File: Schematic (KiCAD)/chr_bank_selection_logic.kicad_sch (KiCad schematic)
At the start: 44 parts

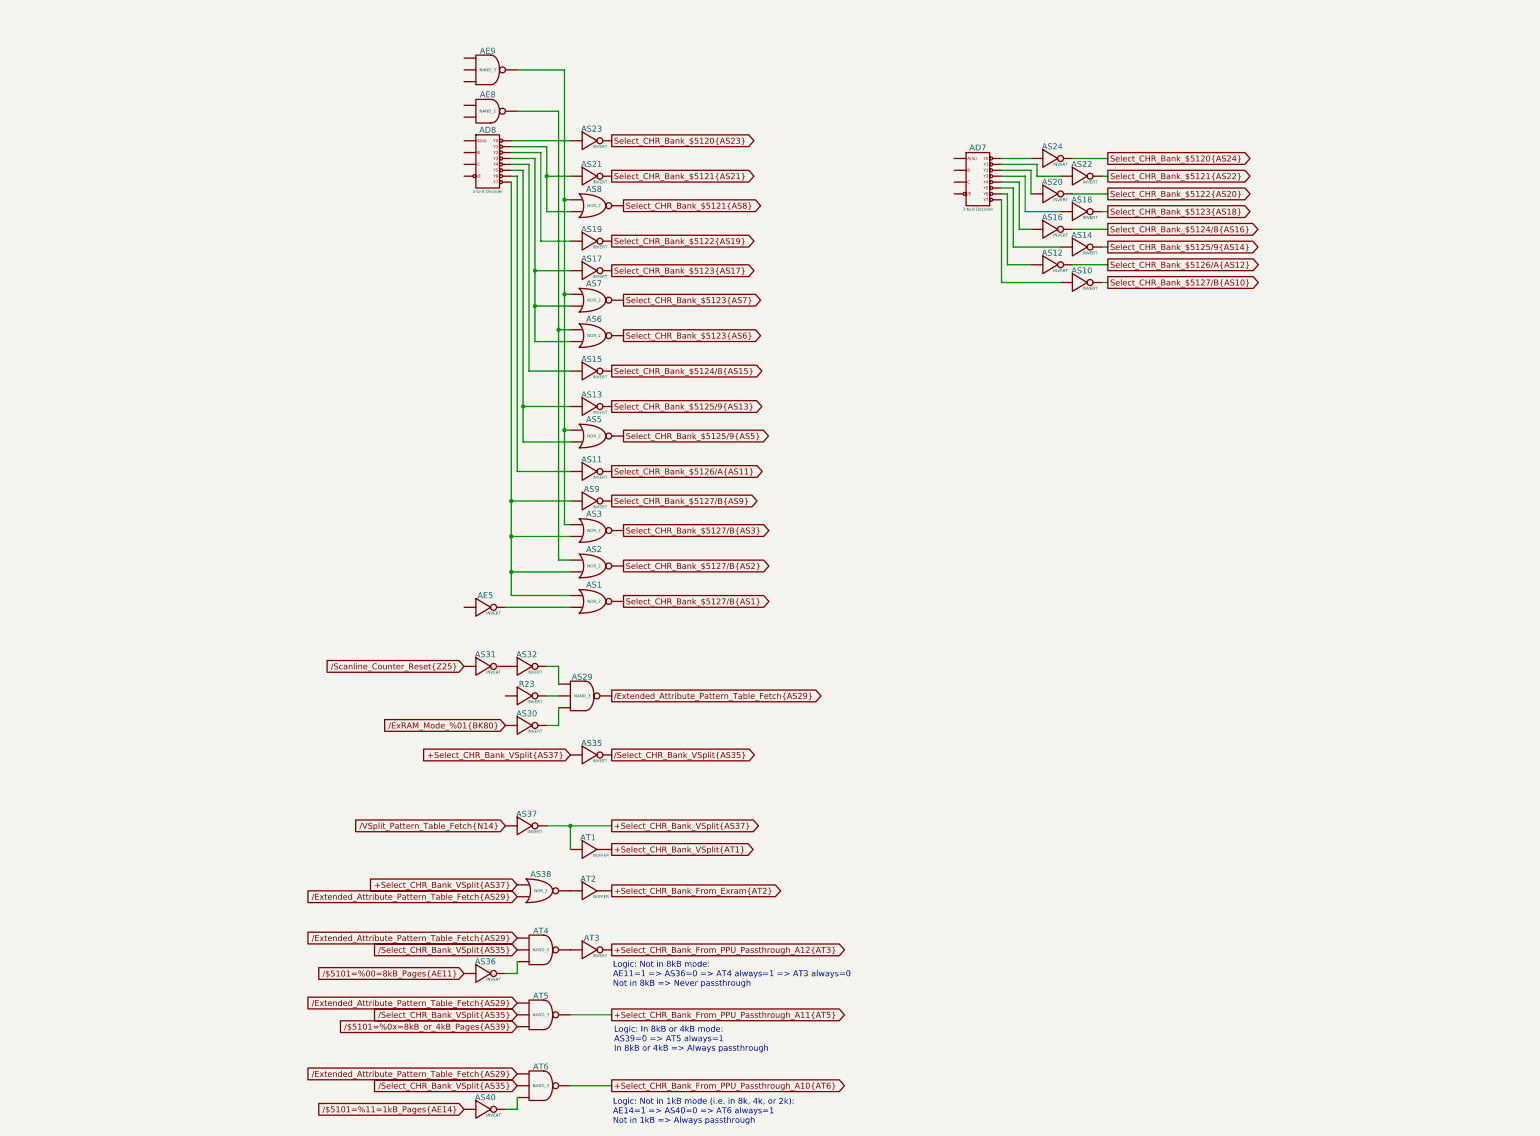
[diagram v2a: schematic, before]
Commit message: - All cells in the left and center areas have now been added into the schematics.  - Changed naming of the PDF files; I was accidentally writing over furrtek's original with my new PDF.
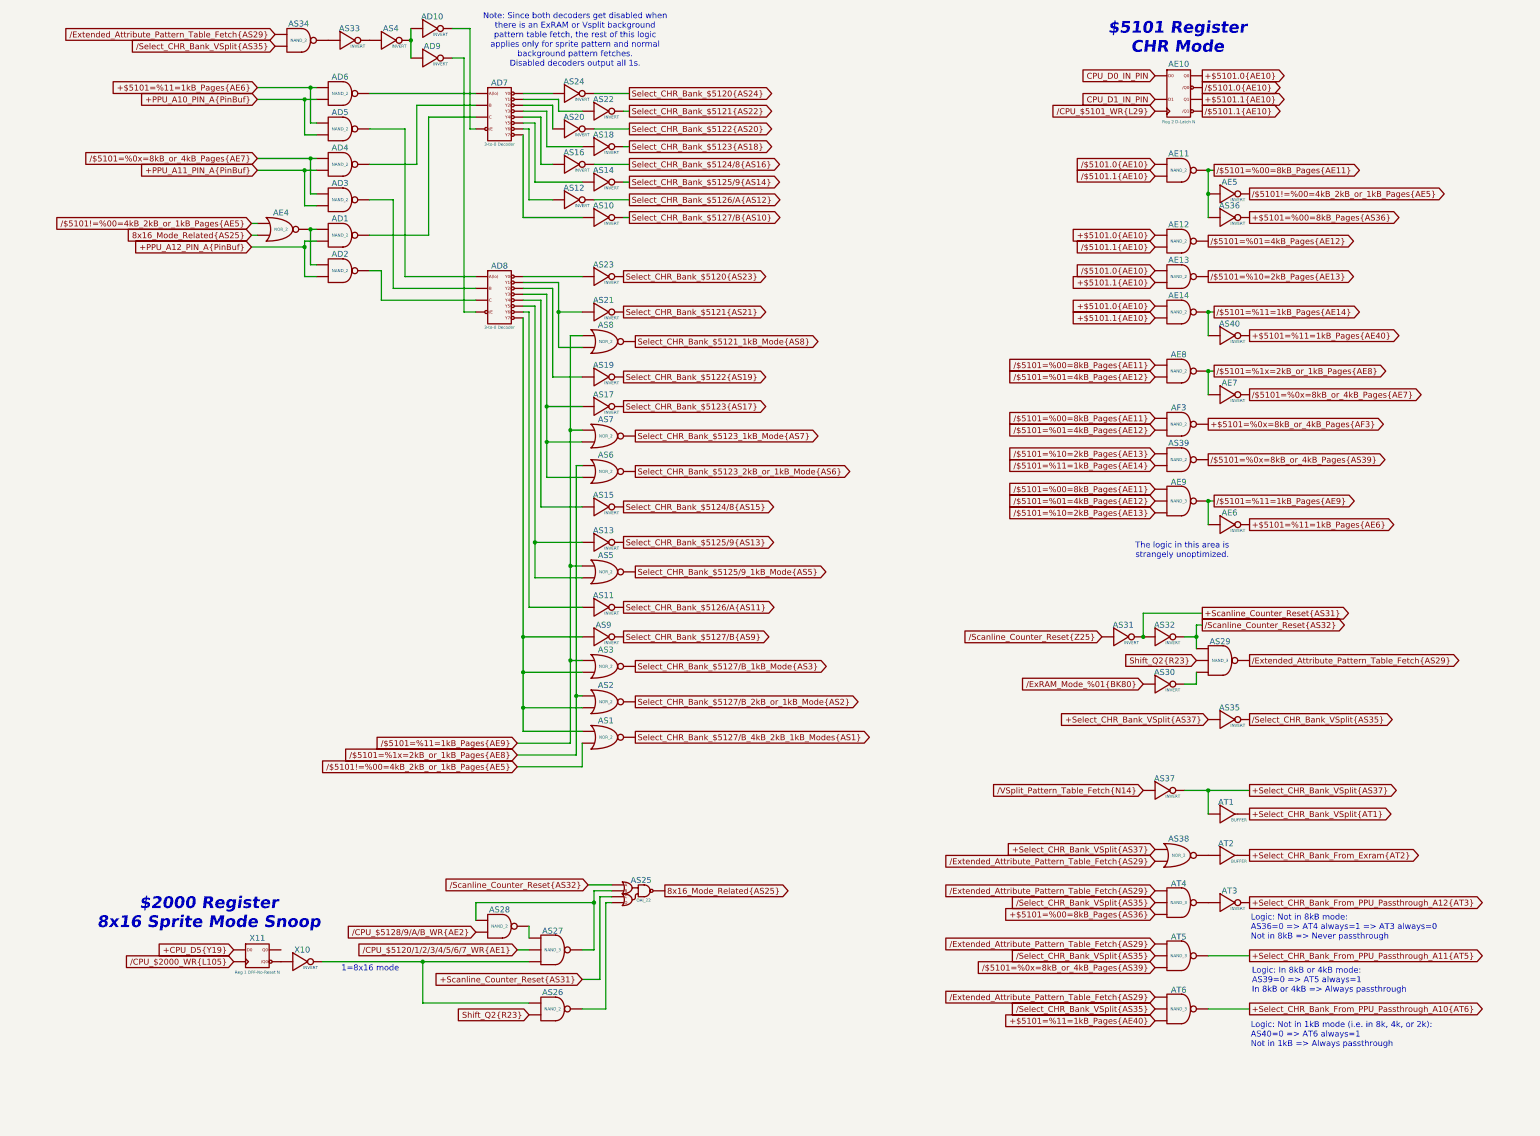
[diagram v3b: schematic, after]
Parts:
- removed R23: INVERT, symbol MMC5:INVERT
- added AD1, AD2, AD3, AD4, AD5, AD6, AE11, AE12, AE13, AE14, AF3, AS26, AS28, AS34, AS39: NAND_2, symbol MMC5:NAND_2
- added AD10, AD9, AE6, AE7, AS33, AS4, X10: INVERT, symbol MMC5:INVERT
- added AE10: Reg 2 D-Latch N, symbol MMC5:Reg_2_D-Latch_N
- added AE4: NOR_2, symbol MMC5:NOR_2
- added AS25: OAI_22, symbol MMC5:OAI_22
- added AS27: NAND_3, symbol MMC5:NAND_3
- added X11: Reg 1 DFF-No-Reset N, symbol MMC5:Reg_1_DFF-No-Reset_N
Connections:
- net Select_CHR_Bank_$5121{AS8} is gone; now on net /$5101=%11=1kB_Pages{AE9}: AS8. (X)
- net Select_CHR_Bank_$5123{AS6} is gone; now on net /$5101=%1x=2kB_or_1kB_Pages{AE8}: AS6. (X)
- net Select_CHR_Bank_$5123{AS7} is gone; now on net /$5101=%11=1kB_Pages{AE9}: AS7. (X)
- net Select_CHR_Bank_$5125/9{AS5} is gone; now on net /$5101=%11=1kB_Pages{AE9}: AS5. (X)
- net Select_CHR_Bank_$5127/B{AS1} is gone; now on net /$5101!=%00=4kB_2kB_or_1kB_Pages{AE5}: AS1. (X)
- net Select_CHR_Bank_$5127/B{AS2} is gone; now on net /$5101=%1x=2kB_or_1kB_Pages{AE8}: AS2. (X)
- net Select_CHR_Bank_$5127/B{AS3} is gone; now on net /$5101=%11=1kB_Pages{AE9}: AS3. (X)
- net /$5101=%00=8kB_Pages{AE11}: now also AE5. (X), AE8. (X), AE9. (X), AE11. (X), AF3. (X)
- net /$5101=%0x=8kB_or_4kB_Pages{AS39}: now also AS39. (X)
- net /$5101=%11=1kB_Pages{AE14}: now also AE14. (X), AS39. (X)
- net /Extended_Attribute_Pattern_Table_Fetch{AS29}: now also AS34. (X)
- net /Select_CHR_Bank_VSplit{AS35}: now also AS34. (X)
- net /$5101!=%00=4kB_2kB_or_1kB_Pages{AE5}: now reaches AE5. (X), AS1. (X)
- net /$5101!=%00=4kB_2kB_or_1kB_Pages{AE5}: now also AE4. (X)
- net /Scanline_Counter_Reset{AS32}: now reaches AS29. (X)
- net /Scanline_Counter_Reset{AS32}: now also AS32. (X), AS25. (X)
- net /$5101=%11=1kB_Pages{AE9}: now reaches AE9. (X), AS3. (X), AS5. (X), AS7. (X), AS8. (X)
- net /$5101=%11=1kB_Pages{AE9}: now also AE6. (X)
- net at AD7. (/Y7): now also AS16. (X); no longer AS14. (X)
- net at AD8. (/Y7): now also AD5. (X); no longer AS23. (X)
- net /$5101=%1x=2kB_or_1kB_Pages{AE8}: now reaches AE8. (X)
- net /$5101=%1x=2kB_or_1kB_Pages{AE8}: now also AE7. (X)
- new net: AD3. (X), AD8. (/Y7)
- new net: AD8. (/Y7), AS1. (X), AS2. (X), AS3. (X), AS9. (X)
- new net: AS33. (X), AS34. (X)
- new net: AS29. (X), AS30. (X)
- new net: AT3. (X), AT4. (X)
- new net: AD10. (X), AD9. (X), AS4. (X)
- new net: AD10. (X), AD7. (/Y7)
- new net: AD8. (/Y7), AS21. (X), AS8. (X)
- new net: AD7. (/Y7), AS14. (X)
- new net: AD7. (/Y7), AS18. (X)
- new net: AD8. (/Y7), AS17. (X), AS6. (X), AS7. (X)
- new net: AD8. (/Y7), AS23. (X)
- new net: AD6. (X), AD7. (/Y7)
- new net: AS33. (X), AS4. (X)
- new net: AS38. (X), AT2. (X)
- new net: AD1. (X), AD2. (X), AE4. (X)
- new net: AD2. (X), AD8. (/Y7)
- new net: AD4. (X), AD7. (/Y7)
- new net: AD8. (/Y7), AD9. (X)
- new net: X10. (X), X11. (/Q0)
- new net: AD7. (/Y7), AS20. (X)
- new net: AD7. (/Y7), AS12. (X)
- new net: AS27. (X), AS28. (X)
- new net: AS25. (X), AS27. (X), AS28. (X)
- new net: AS26. (X), AS27. (X), X10. (X)
- new net: AS25. (X), AS26. (X)
- new net: AD8. (/Y7), AS13. (X), AS5. (X)
- new net: AD8. (/Y7), AS11. (X)
- new net: AD1. (X), AD7. (/Y7)
- new net: AD8. (/Y7), AS15. (X)
- new net: AD8. (/Y7), AS19. (X)
- new net: AD7. (/Y7), AS10. (X)
- new net: AD7. (/Y7), AS22. (X)
- new net: AD7. (/Y7), AS24. (X)
- new net +$5101.0{AE10}: AE10. (/Q1), AE12. (X), AE14. (X)
- new net +$5101.1{AE10}: AE10. (/Q1), AE13. (X), AE14. (X)
- new net +$5101=%00=8kB_Pages{AS36}: AS36. (X), AT4. (X)
- new net +$5101=%0x=8kB_or_4kB_Pages{AF3}: AF3. (X)
- new net +$5101=%11=1kB_Pages{AE40}: AS40. (X), AT6. (X)
- new net +$5101=%11=1kB_Pages{AE6}: AD5. (X), AD6. (X), AE6. (X)
- new net +CPU_D5{Y19}: X11. (/Q0)
- new net +PPU_A10_PIN_A{PinBuf}: AD5. (X), AD6. (X)
- new net +PPU_A11_PIN_A{PinBuf}: AD3. (X), AD4. (X)
- new net +PPU_A12_PIN_A{PinBuf}: AD1. (X), AD2. (X)
- new net +Scanline_Counter_Reset{AS31}: AS25. (X), AS31. (X), AS32. (X)
- new net 8x16_Mode_Related{AS25}: AE4. (X), AS25. (X)
- new net CPU_D0_IN_PIN: AE10. (/Q1)
- new net CPU_D1_IN_PIN: AE10. (/Q1)
- new net Select_CHR_Bank_$5121_1kB_Mode{AS8}: AS8. (X)
- new net Select_CHR_Bank_$5123_1kB_Mode{AS7}: AS7. (X)
- new net Select_CHR_Bank_$5123_2kB_or_1kB_Mode{AS6}: AS6. (X)
- new net Select_CHR_Bank_$5125/9_1kB_Mode{AS5}: AS5. (X)
- new net Select_CHR_Bank_$5127/B_1kB_Mode{AS3}: AS3. (X)
- new net Select_CHR_Bank_$5127/B_2kB_or_1kB_Mode{AS2}: AS2. (X)
- new net Select_CHR_Bank_$5127/B_4kB_2kB_1kB_Modes{AS1}: AS1. (X)
- new net Shift_Q2{R23}: AS26. (X), AS29. (X)
- new net /$5101.0{AE10}: AE10. (/Q1), AE11. (X), AE13. (X)
- new net /$5101.1{AE10}: AE10. (/Q1), AE11. (X), AE12. (X)
- new net /$5101=%01=4kB_Pages{AE12}: AE12. (X), AE8. (X), AE9. (X), AF3. (X)
- new net /$5101=%0x=8kB_or_4kB_Pages{AE7}: AD3. (X), AD4. (X), AE7. (X)
- new net /$5101=%10=2kB_Pages{AE13}: AE13. (X), AE9. (X), AS39. (X)
- new net /CPU_$2000_WR{L105}: X11. (/Q0)
- new net /CPU_$5101_WR{L29}: AE10. (/Q1)
- new net /CPU_$5120/1/2/3/4/5/6/7_WR{AE1}: AS27. (X)
- new net /CPU_$5128/9/A/B_WR{AE2}: AS28. (X)
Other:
- note added: "$2000 Register 8x16 Sprite Mode Snoop"
- note added: "$5101 Register CHR Mode"
- note added: "1=8x16 mode"
- note added: "Logic: Not in 1kB mode (i.e. in 8k, 4k, or 2k): AS40=0 => AT6 always=1 Not in 1kB => Always passthrough"
- note added: "Logic: Not in 8kB mode: AS36=0 => AT4 always=1 => AT3 always=0 Not in 8kB => Never passthrough"
- note added: "Note: Since both decoders get disabled when there is an ExRAM or Vsplit background pattern table fetch, the rest of this logic applies only for sprite pattern and normal background pattern fetches. Disabled decoders output all 1s."
- note added: "The logic in this area is strangely unoptimized."
- note removed: "Logic: Not in 1kB mode (i.e. in 8k, 4k, or 2k): AE14=1 => AS40=0 => AT6 always=1 Not in 1kB => Always passthrough"
- note removed: "Logic: Not in 8kB mode: AE11=1 => AS36=0 => AT4 always=1 => AT3 always=0 Not in 8kB => Never passthrough"
- moved on the sheet: AD7, AD8, AE8, AE9, AS1, AS10, AS11, AS12, AS13, AS14, AS15, AS16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
